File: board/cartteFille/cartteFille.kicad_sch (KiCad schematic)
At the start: 13 parts, among them U1 LM358, U20 MCP23018-E/SS

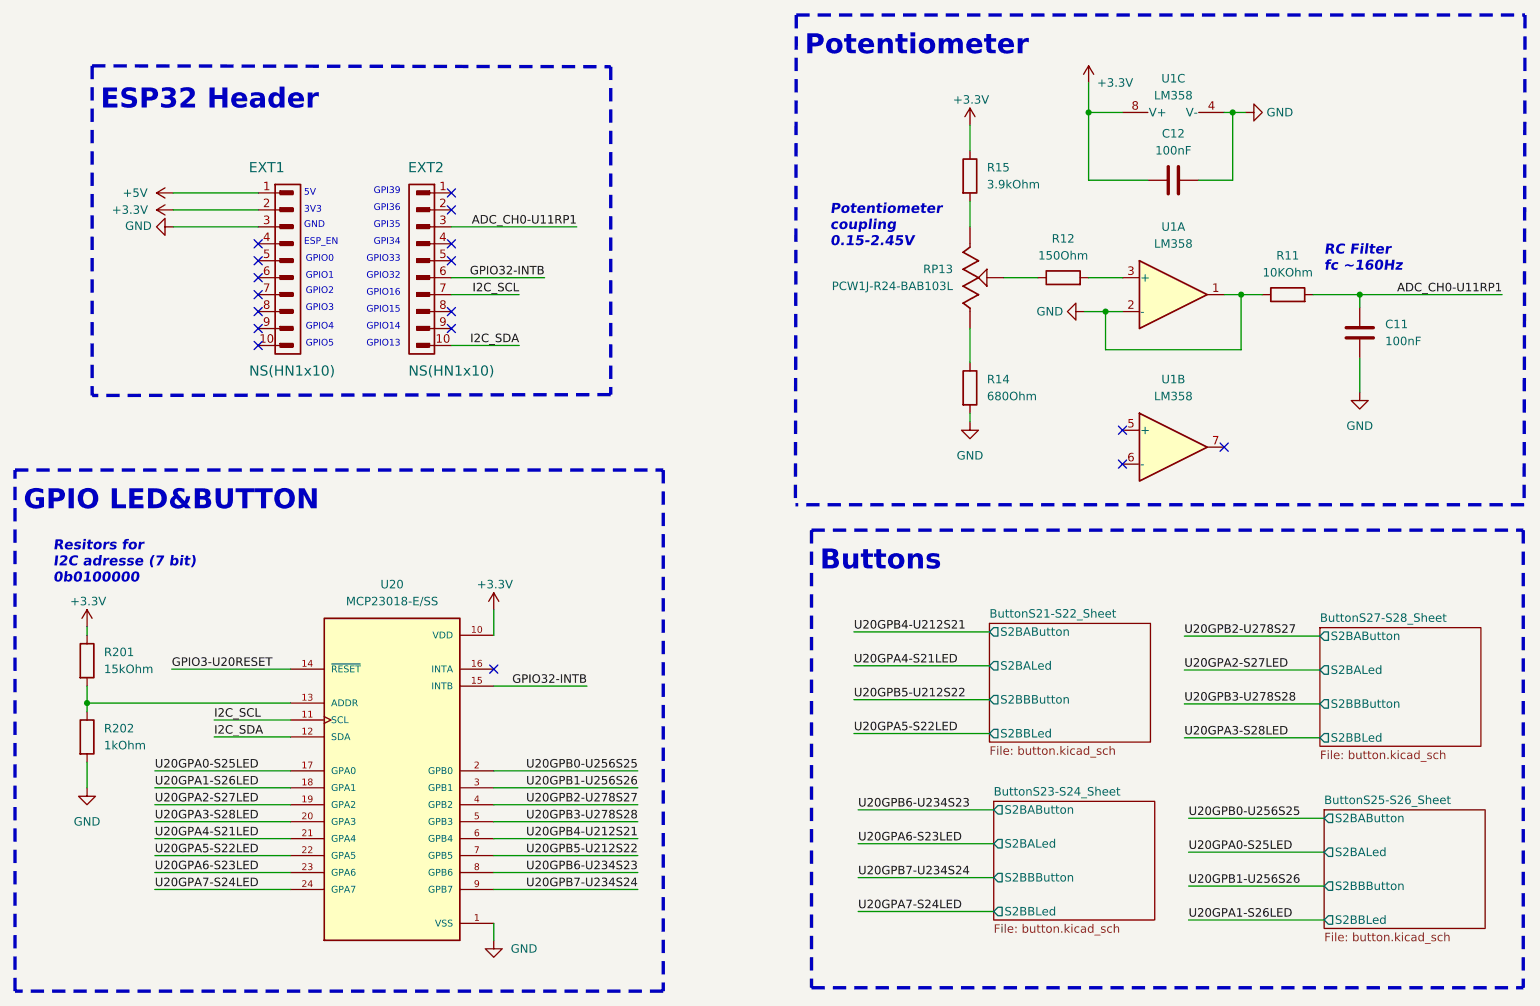
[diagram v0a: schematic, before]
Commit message: pcb presque final
Les trous de montages doivent être réajuster
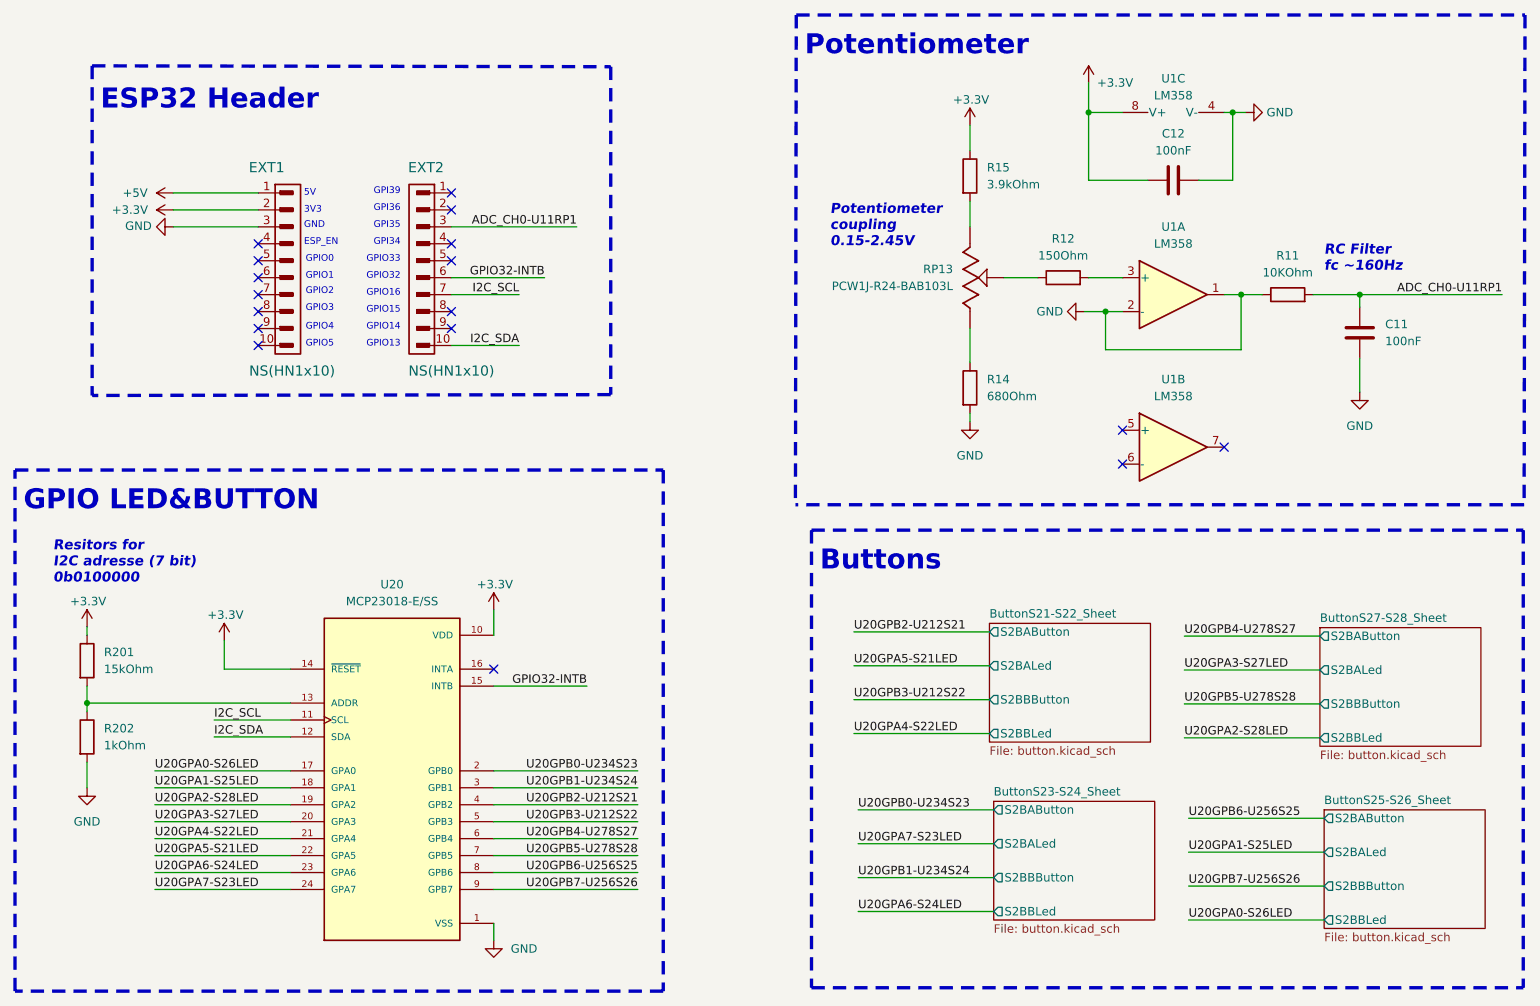
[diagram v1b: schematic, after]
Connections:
- net GPIO3-U20RESET is gone; now on net +3V3: U20.14 (~{RESET})
- net U20GPA0-S25LED renamed U20GPA0-S26LED
- net U20GPA1-S26LED renamed U20GPA1-S25LED
- net U20GPA2-S27LED renamed U20GPA2-S28LED
- net U20GPA3-S28LED renamed U20GPA3-S27LED
- net U20GPA4-S21LED renamed U20GPA4-S22LED
- net U20GPA5-S22LED renamed U20GPA5-S21LED
- net U20GPA6-S23LED renamed U20GPA6-S24LED
- net U20GPA7-S24LED renamed U20GPA7-S23LED
- net U20GPB0-U256S25 renamed U20GPB0-U234S23
- net U20GPB1-U256S26 renamed U20GPB1-U234S24
- net U20GPB2-U278S27 renamed U20GPB2-U212S21
- net U20GPB3-U278S28 renamed U20GPB3-U212S22
- net U20GPB4-U212S21 renamed U20GPB4-U278S27
- net U20GPB5-U212S22 renamed U20GPB5-U278S28
- net U20GPB6-U234S23 renamed U20GPB6-U256S25
- net U20GPB7-U234S24 renamed U20GPB7-U256S26
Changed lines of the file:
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@@
-    (stroke (width 0) (type default) (color 0 0 0 0))
-  )
-  (wire (pts (xy 68.58 115.316) (xy 86.36 115.316))
     (stroke (width 0) (type default) (color 0 0 0 0))
   )
@@
     (stroke (width 0) (type default) (color 0 0 0 0))
   )
+  (wire (pts (xy 76.454 110.998) (xy 76.454 115.316))
+    (stroke (width 0) (type default) (color 0 0 0 0))
+  )
   (wire (pts (xy 220.345 120.523) (xy 240.665 120.523))
     (stroke (width 0) (type default) (color 0 0 0 0))
@@
   )
   (wire (pts (xy 129.286 49.022) (xy 110.49 49.022))
+    (stroke (width 0) (type default) (color 0 0 0 0))
+  )
+  (wire (pts (xy 76.454 115.316) (xy 86.36 115.316))
     (stroke (width 0) (type default) (color 0 0 0 0))
   )
@@
     (effects (font (size 1.27 1.27)) (justify right bottom))
   )
-  (label "U20GPB1-U256S26" (at 220.98 147.828 0)
-    (effects (font (size 1.27 1.27)) (justify left bottom))
+  (label "U20GPB7-U256S26" (at 220.98 147.828 0)
+    (effects (font (size 1.27 1.27)) (justify left bottom))
+  )
+  (label "U20GPB7-U256S26" (at 138.43 148.336 180)
+    (effects (font (size 1.27 1.27)) (justify right bottom))
   )
   (label "I2C_SCL" (at 120.65 59.182 180)
     (effects (font (size 1.27 1.27)) (justify right bottom))
   )
-  (label "U20GPA4-S21LED" (at 66.04 140.716 0)
-    (effects (font (size 1.27 1.27)) (justify left bottom))
-  )
-  (label "U20GPA5-S22LED" (at 170.815 124.968 0)
-    (effects (font (size 1.27 1.27)) (justify left bottom))
-  )
-  (label "U20GPA5-S22LED" (at 66.04 143.256 0)
-    (effects (font (size 1.27 1.27)) (justify left bottom))
-  )
-  (label "U20GPB2-U278S27" (at 220.345 110.363 0)
+  (label "U20GPA4-S22LED" (at 66.04 140.716 0)
+    (effects (font (size 1.27 1.27)) (justify left bottom))
+  )
+  (label "U20GPA4-S22LED" (at 170.815 124.968 0)
+    (effects (font (size 1.27 1.27)) (justify left bottom))
+  )
+  (label "U20GPA5-S21LED" (at 66.04 143.256 0)
+    (effects (font (size 1.27 1.27)) (justify left bottom))
+  )
+  (label "U20GPB4-U278S27" (at 220.345 110.363 0)
     (effects (font (size 1.27 1.27)) (justify left bottom))
   )
@@
     (effects (font (size 1.27 1.27)) (justify right bottom))
   )
-  (label "U20GPA6-S23LED" (at 171.45 141.478 0)
-    (effects (font (size 1.27 1.27)) (justify left bottom))
-  )
-  (label "U20GPB4-U212S21" (at 138.43 140.716 180)
-    (effects (font (size 1.27 1.27)) (justify right bottom))
+  (label "U20GPA7-S23LED" (at 171.45 141.478 0)
+    (effects (font (size 1.27 1.27)) (justify left bottom))
   )
   (label "ADC_CH0-U11RP1" (at 129.286 49.022 180)
     (effects (font (size 1.27 1.27)) (justify right bottom))
   )
-  (label "U20GPA1-S26LED" (at 66.04 133.096 0)
-    (effects (font (size 1.27 1.27)) (justify left bottom))
-  )
-  (label "U20GPA3-S28LED" (at 66.04 138.176 0)
-    (effects (font (size 1.27 1.27)) (justify left bottom))
-  )
-  (label "U20GPB7-U234S24" (at 171.45 146.558 0)
-    (effects (font (size 1.27 1.27)) (justify left bottom))
-  )
-  (label "GPIO3-U20RESET" (at 68.58 115.316 0)
-    (effects (font (size 1.27 1.27)) (justify left bottom))
-  )
-  (label "U20GPB3-U278S28" (at 220.345 120.523 0)
-    (effects (font (size 1.27 1.27)) (justify left bottom))
-  )
-  (label "U20GPA1-S26LED" (at 220.98 152.908 0)
-    (effects (font (size 1.27 1.27)) (justify left bottom))
+  (label "U20GPB2-U212S21" (at 138.43 135.636 180)
+    (effects (font (size 1.27 1.27)) (justify right bottom))
+  )
+  (label "U20GPB3-U212S22" (at 138.43 138.176 180)
+    (effects (font (size 1.27 1.27)) (justify right bottom))
+  )
+  (label "U20GPA1-S25LED" (at 66.04 133.096 0)
+    (effects (font (size 1.27 1.27)) (justify left bottom))
+  )
+  (label "U20GPA3-S27LED" (at 66.04 138.176 0)
+    (effects (font (size 1.27 1.27)) (justify left bottom))
+  )
+  (label "U20GPB1-U234S24" (at 171.45 146.558 0)
+    (effects (font (size 1.27 1.27)) (justify left bottom))
+  )
+  (label "U20GPB5-U278S28" (at 220.345 120.523 0)
+    (effects (font (size 1.27 1.27)) (justify left bottom))
+  )
+  (label "U20GPA0-S26LED" (at 220.98 152.908 0)
+    (effects (font (size 1.27 1.27)) (justify left bottom))
+  )
+  (label "U20GPB5-U278S28" (at 138.43 143.256 180)
+    (effects (font (size 1.27 1.27)) (justify right bottom))
   )
   (label "I2C_SDA" (at 74.93 125.476 0)
     (effects (font (size 1.27 1.27)) (justify left bottom))
   )
-  (label "U20GPA7-S24LED" (at 66.04 148.336 0)
+  (label "U20GPA7-S23LED" (at 66.04 148.336 0)
     (effects (font (size 1.27 1.27)) (justify left bottom))
   )
@@
     (effects (font (size 1.27 1.27)) (justify right bottom))
   )
+  (label "U20GPB4-U278S27" (at 138.43 140.716 180)
+    (effects (font (size 1.27 1.27)) (justify right bottom))
+  )
+  (label "U20GPB6-U256S25" (at 138.43 145.796 180)
+    (effects (font (size 1.27 1.27)) (justify right bottom))
+  )
+  (label "U20GPB1-U234S24" (at 138.43 133.096 180)
+    (effects (font (size 1.27 1.27)) (justify right bottom))
+  )
   (label "I2C_SCL" (at 74.93 122.936 0)
     (effects (font (size 1.27 1.27)) (justify left bottom))
   )
-  (label "U20GPB0-U256S25" (at 220.98 137.668 0)
-    (effects (font (size 1.27 1.27)) (justify left bottom))
-  )
-  (label "U20GPB2-U278S27" (at 138.43 135.636 180)
-    (effects (font (size 1.27 1.27)) (justify right bottom))
-  )
-  (label "U20GPA3-S28LED" (at 220.345 125.603 0)
-    (effects (font (size 1.27 1.27)) (justify left bottom))
-  )
-  (label "U20GPA0-S25LED" (at 220.98 142.748 0)
-    (effects (font (size 1.27 1.27)) (justify left bottom))
-  )
-  (label "U20GPA4-S21LED" (at 170.815 114.808 0)
-    (effects (font (size 1.27 1.27)) (justify left bottom))
-  )
-  (label "U20GPB3-U278S28" (at 138.43 138.176 180)
-    (effects (font (size 1.27 1.27)) (justify right bottom))
-  )
-  (label "U20GPB6-U234S23" (at 138.43 145.796 180)
-    (effects (font (size 1.27 1.27)) (justify right bottom))
-  )
-  (label "U20GPB6-U234S23" (at 171.45 136.398 0)
-    (effects (font (size 1.27 1.27)) (justify left bottom))
-  )
-  (label "U20GPA6-S23LED" (at 66.04 145.796 0)
-    (effects (font (size 1.27 1.27)) (justify left bottom))
-  )
-  (label "U20GPA7-S24LED" (at 171.45 151.638 0)
-    (effects (font (size 1.27 1.27)) (justify left bottom))
-  )
-  (label "U20GPB1-U256S26" (at 138.43 133.096 180)
-    (effects (font (size 1.27 1.27)) (justify right bottom))
-  )
-  (label "U20GPB0-U256S25" (at 138.43 130.556 180)
-    (effects (font (size 1.27 1.27)) (justify right bottom))
-  )
-  (label "U20GPB5-U212S22" (at 138.43 143.256 180)
-    (effects (font (size 1.27 1.27)) (justify right bottom))
-  )
-  (label "U20GPB4-U212S21" (at 170.815 109.728 0)
+  (label "U20GPB6-U256S25" (at 220.98 137.668 0)
+    (effects (font (size 1.27 1.27)) (justify left bottom))
+  )
+  (label "U20GPA2-S28LED" (at 220.345 125.603 0)
+    (effects (font (size 1.27 1.27)) (justify left bottom))
+  )
+  (label "U20GPA1-S25LED" (at 220.98 142.748 0)
+    (effects (font (size 1.27 1.27)) (justify left bottom))
+  )
+  (label "U20GPA5-S21LED" (at 170.815 114.808 0)
+    (effects (font (size 1.27 1.27)) (justify left bottom))
+  )
+  (label "U20GPB0-U234S23" (at 171.45 136.398 0)
+    (effects (font (size 1.27 1.27)) (justify left bottom))
+  )
+  (label "U20GPA6-S24LED" (at 66.04 145.796 0)
+    (effects (font (size 1.27 1.27)) (justify left bottom))
+  )
+  (label "U20GPA6-S24LED" (at 171.45 151.638 0)
+    (effects (font (size 1.27 1.27)) (justify left bottom))
+  )
+  (label "U20GPB0-U234S23" (at 138.43 130.556 180)
+    (effects (font (size 1.27 1.27)) (justify right bottom))
+  )
+  (label "U20GPB2-U212S21" (at 170.815 109.728 0)
     (effects (font (size 1.27 1.27)) (justify left bottom))
   )
@@
     (effects (font (size 1.27 1.27)) (justify right bottom))
   )
-  (label "U20GPB5-U212S22" (at 170.815 119.888 0)
-    (effects (font (size 1.27 1.27)) (justify left bottom))
-  )
-  (label "U20GPA2-S27LED" (at 220.345 115.443 0)
-    (effects (font (size 1.27 1.27)) (justify left bottom))
-  )
-  (label "U20GPA2-S27LED" (at 66.04 135.636 0)
-    (effects (font (size 1.27 1.27)) (justify left bottom))
-  )
-  (label "U20GPA0-S25LED" (at 66.04 130.556 0)
-    (effects (font (size 1.27 1.27)) (justify left bottom))
-  )
-  (label "U20GPB7-U234S24" (at 138.43 148.336 180)
-    (effects (font (size 1.27 1.27)) (justify right bottom))
+  (label "U20GPB3-U212S22" (at 170.815 119.888 0)
+    (effects (font (size 1.27 1.27)) (justify left bottom))
+  )
+  (label "U20GPA3-S27LED" (at 220.345 115.443 0)
+    (effects (font (size 1.27 1.27)) (justify left bottom))
+  )
+  (label "U20GPA2-S28LED" (at 66.04 135.636 0)
+    (effects (font (size 1.27 1.27)) (justify left bottom))
+  )
+  (label "U20GPA0-S26LED" (at 66.04 130.556 0)
+    (effects (font (size 1.27 1.27)) (justify left bottom))
+  )
+  (symbol (lib_id "ESP32-PoE-ISO_Rev_H:+3.3V") (at 76.454 110.998 0) (unit 1)
+    (in_bom yes) (on_board yes)
+    (property "Reference" "#PWR0154" (id 0) (at 76.454 114.808 0)
+      (effects (font (size 1.27 1.27)) hide)
+    )
+    (property "Value" "+3.3V" (id 1) (at 73.914 107.188 0)
+      (effects (font (size 1.27 1.27)) (justify left))
+    )
+    (property "Footprint" "" (id 2) (at 76.454 110.998 0)
+      (effects (font (size 1.524 1.524)))
+    )
+    (property "Datasheet" "" (id 3) (at 76.454 110.998 0)
+      (effects (font (size 1.524 1.524)))
+    )
+    (pin "1")
   )
   (symbol (lib_id "power:GND") (at 229.489 31.877 90) (unit 1)
@@
       (reference "#PWR0153") (unit 1) (value "+5V") (footprint "")
     )
+    (path "/0574e075-2594-4438-bbc0-8c8fc583653d"
+      (reference "#PWR0154") (unit 1) (value "+3.3V") (footprint "")
+    )
     (path "/13ff9bef-e3b3-4f37-bf8c-71465cfffb2a"

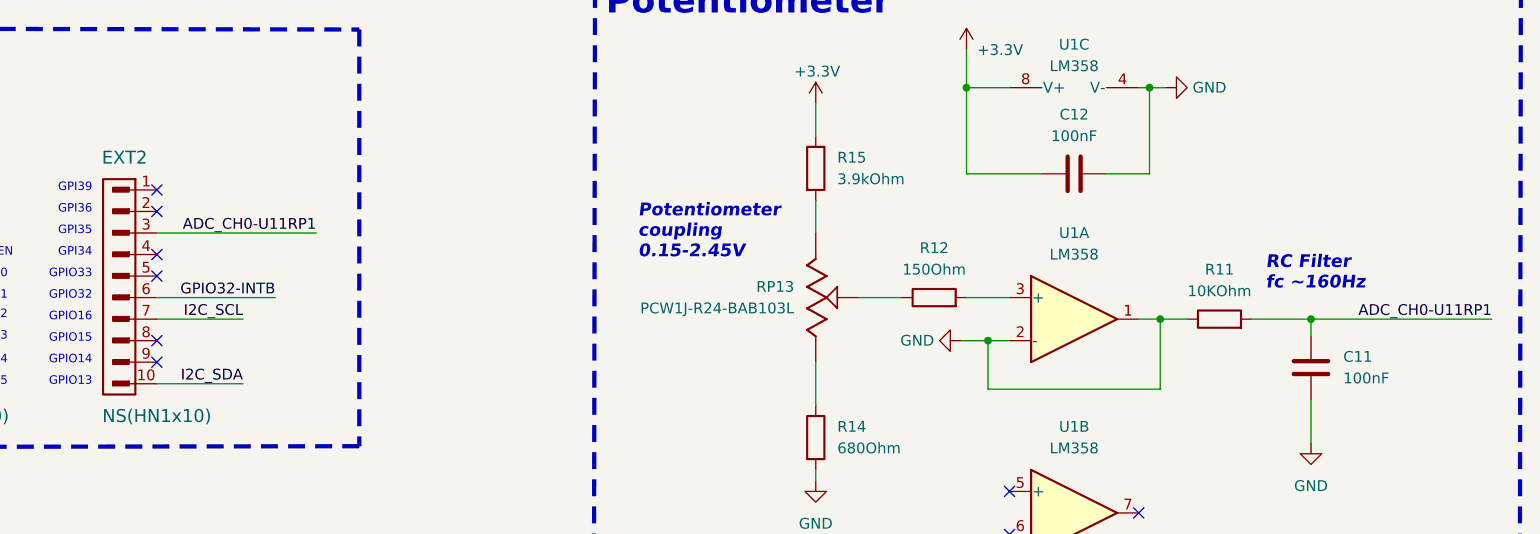
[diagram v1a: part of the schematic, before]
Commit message: commit_V2_PCB
seciond version of pcb final version with gerbert fils
ZIP of the gerber = gerbert_V2
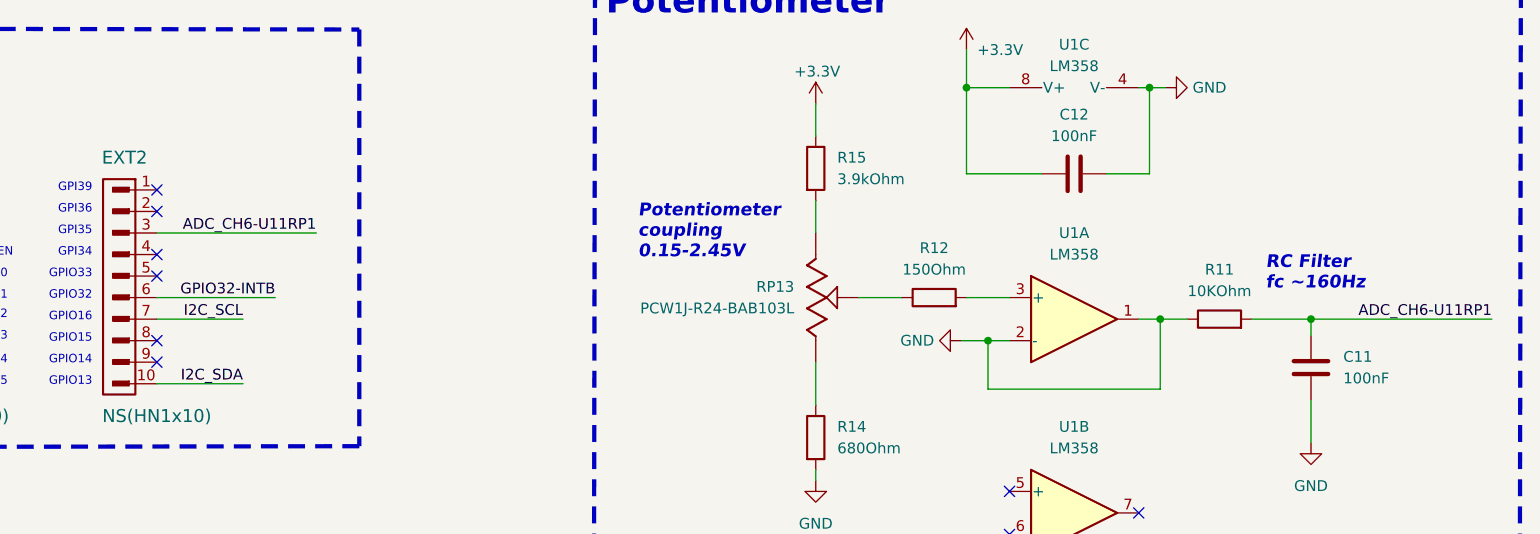
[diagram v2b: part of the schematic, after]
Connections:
- net ADC_CH0-U11RP1 renamed ADC_CH6-U11RP1
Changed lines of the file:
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@@
     (effects (font (size 1 1)) (justify right bottom))
   )
-  (label "ADC_CH0-U11RP1" (at 267.97 59.182 180)
+  (label "ADC_CH6-U11RP1" (at 267.97 59.182 180)
     (effects (font (size 1.27 1.27)) (justify right bottom))
   )
@@
     (effects (font (size 1.27 1.27)) (justify left bottom))
   )
-  (label "ADC_CH0-U11RP1" (at 129.286 49.022 180)
+  (label "ADC_CH6-U11RP1" (at 129.286 49.022 180)
     (effects (font (size 1.27 1.27)) (justify right bottom))
   )
